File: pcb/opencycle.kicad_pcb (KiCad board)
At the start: 4 copper layers, 46 x 80 mm, 65 parts, among them J1 USB-C, J2 Battery, J3 LS027B7DH01, J4 SWD, SW1 Page/lap, SW2 Start/stop, SW3 Power, U1 MDBT50Q-1MV2, U10 SN74LV1T34DCK, U11 SN74LV1T34DCK, U12 BMP280, U13 LIS3DH, U14 MAX98357A, U2 MAX-M10S, U3 W25Q128JVSIQ, U4 MCP73831-2, U5 XC6220B331MR, U6 TPS61220DCK, U7 SN74LV1T34DCK, U8 SN74LV1T34DCK, U9 SN74LV1T34DCK

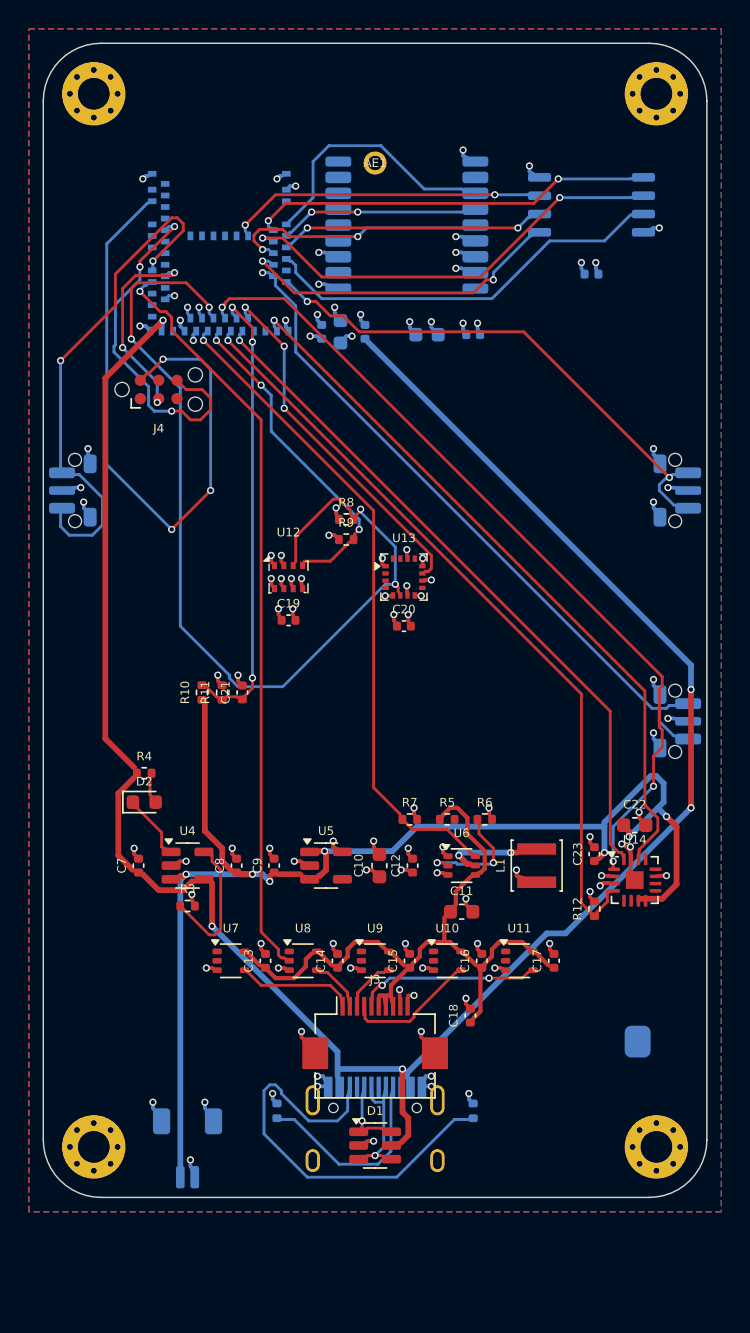
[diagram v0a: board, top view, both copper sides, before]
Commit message: pcb: text-generated local footprints (fixes pads stacked at the origin), work-in-progress routed board + DRC report
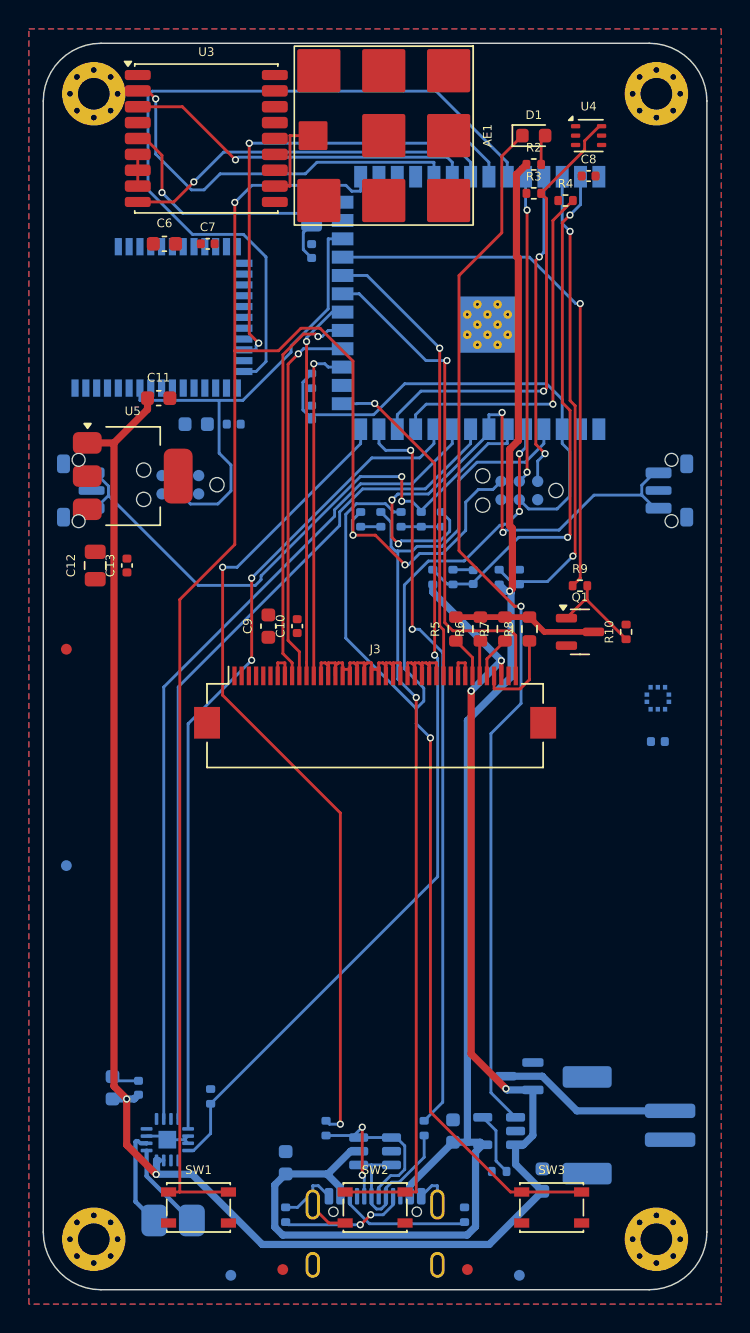
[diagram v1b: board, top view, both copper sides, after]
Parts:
- removed C21, C23: 100nF, C_0402_1005Metric
- removed C22: 10uF, C_0603_1608Metric
- removed L1: 4.7uH, L_Sunlord_SWPA3012S
- removed U10, U11, U9: SN74LV1T34DCK, SOT-353_SC-70-5
- removed U12: BMP280, Bosch_LGA-8_2x2.5mm_P0.65mm_ClockwisePinNumbering
- removed U13: LIS3DH, LGA-16_3x3mm_P0.5mm
- removed U14: MAX98357A, TQFN-16-1EP_3x3mm_P0.5mm_EP1.23x1.23mm
- added FID1: Fiducial, Fiducial_0.75mm_Mask1.5mm, F.Cu at (19.6, 88.0)
- added FID2: Fiducial, Fiducial_0.75mm_Mask1.5mm, F.Cu at (32.4, 88.0)
- added FID3: Fiducial, Fiducial_0.75mm_Mask1.5mm, F.Cu at (4.60, 45.0)
- added FID4: Fiducial, Fiducial_0.75mm_Mask1.5mm, B.Cu at (16.0, 88.4)
- added FID5: Fiducial, Fiducial_0.75mm_Mask1.5mm, B.Cu at (36.0, 88.4)
- added FID6: Fiducial, Fiducial_0.75mm_Mask1.5mm, B.Cu at (4.60, 60.0)
- added J5: Console, Tag-Connect_TC2030-IDC-NL_2x03_P1.27mm_Vertical, B.Cu at (36.0, 34.0)
- added Q1: DMG2302U, SOT-23, F.Cu at (40.2, 43.8)
- added Q2: DMG2305UX, SOT-23, B.Cu at (36.0, 74.6)
- added R13: 0R, R_0402_1005Metric, B.Cu at (22.6, 78.2)
- added R14: 0R, R_0402_1005Metric, B.Cu at (29.4, 78.2)
- added R15: 2k, R_0402_1005Metric, B.Cu at (34.6, 81.2)
- added R16: 1M, R_0402_1005Metric, B.Cu at (30.0, 40.0)
- added R17: 1M, R_0402_1005Metric, B.Cu at (31.4, 40.0)
- added R18: 100k, R_0402_1005Metric, B.Cu at (34.6, 40.0)
- added R19: 100k, R_0402_1005Metric, B.Cu at (36.0, 40.0)
- added R20: 100k, R_0402_1005Metric, B.Cu at (14.6, 76.0)
- added R21: 10k, R_0402_1005Metric, B.Cu at (25.0, 36.0)
- added R22: 10k, R_0402_1005Metric, B.Cu at (26.4, 36.0)
- added R23: 10k, R_0402_1005Metric, B.Cu at (27.8, 36.0)
- added R24: 10k, R_0402_1005Metric, B.Cu at (29.2, 36.0)
- added R25: 10k, R_0402_1005Metric, B.Cu at (30.6, 36.0)
- added SW4: SKRTLAE010, SW_Push_1P1T-MP_NO_Horizontal_Alps_SKRTLAE010, B.Cu at (5.45, 34.0)
- added SW5: SKRTLAE010, SW_Push_1P1T-MP_NO_Horizontal_Alps_SKRTLAE010, B.Cu at (46.5, 34.0)
- AE1: value GNSS patch 15x15x4 -> DSGP.1575.12.4.A.02; footprint Patch_15x15_Feed -> Taoglas_DSGP.1575.12.4.A.02_12x12mm
- C1: value 10uF -> 22uF; footprint C_0603_1608Metric -> C_0805_2012Metric
- C10: value 10uF -> 100nF; footprint C_0603_1608Metric -> C_0402_1005Metric
- C12: value 4.7uF -> 22uF; footprint C_0402_1005Metric -> C_0805_2012Metric
- C14, C15, C16: value 100nF -> 4.7uF; footprint C_0402_1005Metric -> C_0603_1608Metric; moved to B.Cu
- C17, C19, C20: moved to B.Cu
- C18: value 1uF -> 10uF; footprint C_0402_1005Metric -> C_0603_1608Metric; moved to B.Cu
- C3: value 4.7uF -> 1uF
- C6: value 100nF -> 10uF; footprint C_0402_1005Metric -> C_0603_1608Metric; moved to F.Cu
- C7, C8: value 4.7uF -> 100nF
- C9: value 1uF -> 10uF; footprint C_0402_1005Metric -> C_0603_1608Metric
- D1: value USBLC6-2SC6 -> Green; footprint SOT-23-6 -> LED_0603_1608Metric
- D2: value Green -> USBLC6-2SC6; footprint LED_0603_1608Metric -> SOT-23-6; moved to B.Cu
- J1: value USB-C -> USB4105-GF-A; footprint USB_C_Receptacle_HRO_TYPE-C-31-M-12 -> USB_C_Receptacle_GCT_USB4105-xx-A_16P_TopMnt_Horizontal
- J2: value Battery -> S2B-PH-SM4-TB; footprint JST_SH_SM02B-SRSS-TB_1x02-1MP_P1.00mm_Horizontal -> JST_PH_S2B-PH-SM4-TB_1x02-1MP_P2.00mm_Horizontal
- J3: value LS027B7DH01 -> FH12-40S-0.5SH(55); footprint Hirose_FH12-10S-0.5SH_1x10-1MP_P0.50mm_Horizontal -> Hirose_FH12-40S-0.5SH_1x40-1MP_P0.50mm_Horizontal
- J4: value SWD -> SWD (BL652); moved to B.Cu
- LS1: value 8R 1W 11x15 -> CMS-151125-078L100
- R1: value 5.1k -> 10k
- R10: value 1M -> 100k
- R11: value 1M -> 5.1k; moved to B.Cu
- R12: value 100k -> 5.1k; moved to B.Cu
- R2: value 5.1k -> 1k; moved to F.Cu
- R3: value 2k -> 4.7k
- R4: value 1k -> 4.7k
- R5, R7: value 1M -> 33R; footprint R_0402_1005Metric -> R_0603_1608Metric
- R6: value 110k -> 33R; footprint R_0402_1005Metric -> R_0603_1608Metric
- R8: value 4.7k -> 33R; footprint R_0402_1005Metric -> R_0603_1608Metric
- R9: value 4.7k -> 100R
- SW1: value Page/lap -> PTS810; footprint SW_Push_1P1T-MP_NO_Horizontal_Alps_SKRTLAE010 -> SW_SPST_PTS810; moved to F.Cu
- SW2: value Start/stop -> PTS810; footprint SW_Push_1P1T-MP_NO_Horizontal_Alps_SKRTLAE010 -> SW_SPST_PTS810; moved to F.Cu
- SW3: value Power -> PTS810; footprint SW_Push_1P1T-MP_NO_Horizontal_Alps_SKRTLAE010 -> SW_SPST_PTS810; moved to F.Cu
- U1: value MDBT50Q-1MV2 -> ESP32-S3-WROOM-1-N16R8; footprint Raytac_MDBT50Q -> ESP32-S3-WROOM-1
- U2: value MAX-M10S -> BL652-SA-01; footprint ublox_MAX -> Laird_BL652
- U3: value W25Q128JVSIQ -> MAX-M10S; footprint SOIC-8_5.23x5.23mm_P1.27mm -> ublox_MAX; moved to F.Cu
- U4: value MCP73831-2 -> LTR-303ALS-01; footprint SOT-23-5 -> Lite-On_LTR-303ALS-01
- U5: value XC6220B331MR -> AP7361C-33E; footprint SOT-23-5 -> SOT-223-3_TabPin2
- U6: value TPS61220DCK -> MCP73831-2; footprint SOT-363_SC-70-6 -> SOT-23-5; moved to B.Cu
- U7: value SN74LV1T34DCK -> MAX98357A; footprint SOT-353_SC-70-5 -> TQFN-16-1EP_3x3mm_P0.5mm_EP1.23x1.23mm; moved to B.Cu
- U8: value SN74LV1T34DCK -> BMP581; footprint SOT-353_SC-70-5 -> Bosch_LGA-10_2x2mm_P0.5mm_BMP581; moved to B.Cu
- moved D1 70.9 mm to (37.0, 9.40)
- moved R2 65.7 mm to (37.0, 11.4), turned to 0 degrees
- moved SW1 59.7 mm to (13.8, 83.7), turned to 0 degrees
- moved SW3 59.7 mm to (38.2, 83.7), turned to 0 degrees
- moved U4 57.7 mm to (40.8, 9.40)
- moved R3 54.9 mm to (37.0, 13.4)
- moved C8 53.7 mm to (40.8, 12.2), turned to 0 degrees
- moved R1 50.7 mm to (21.6, 26.4)
- moved R4 49.3 mm to (39.2, 13.9)
- moved C7 43.4 mm to (14.4, 16.9), turned to 0 degrees
- moved C11 41.3 mm to (11.0, 27.6)
- moved SW2 39.6 mm to (26.0, 83.7), turned to 0 degrees
- moved R11 36.5 mm to (19.8, 84.2)
- moved LS1 34.5 mm to (12.0, 84.6)
- moved C19 34.0 mm to (9.60, 75.4), turned to 90 degrees
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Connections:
- C11 pad 1: +5V_DISP -> VBAT
- C13 pad 1: +5V_DISP -> +3V3
- C14 pad 1: +5V_DISP -> VBUS
- C15 pad 1: +5V_DISP -> VBUS
- C16 pad 1: +5V_DISP -> VBAT
- C17 pad 1: +5V_DISP -> VBAT_SENSE
- C18 pad 1: +5V_DISP -> VBAT
- C19 pad 1: +3V3 -> VBAT
- C3 pad 1: VBUS -> ESP_EN
- C7 pad 1: VBUS -> +3V3
- C8 pad 1: VBAT -> +3V3
- C9 pad 1: VBAT -> +3V3
- D1 pad 1: USB_DP_C -> CHG_STAT
- D1 pad 2: GND -> LED_A
- D2 pad 1: CHG_STAT -> USB_DP_C
- D2 pad 2: LED_A -> GND
- J2 pad 1: VBAT -> GND
- J2 pad 2: GND -> BATT+
- J3 pad 1: DISP_SCLK -> GND
- J3 pad 10: GND -> LCD_CS
- J3 pad 2: DISP_SI -> (no net)
- J3 pad 3: DISP_SCS -> (no net)
- J3 pad 4: DISP_EXTCOM -> (no net)
- J3 pad 5: DISP_ON -> (no net)
- J3 pad 6: +5V_DISP -> (no net)
- J3 pad 7: +5V_DISP -> +3V3
- J3 pad 8: +5V_DISP -> +3V3
- J3 pad 9: GND -> LCD_MOSI
- J4 pad 2: SWDIO -> BLE_SWDIO
- J4 pad 3: ~RESET -> BLE_RST
- J4 pad 4: SWDCLK -> BLE_SWDCLK
- J4 pad 6: SWO -> (no net)
- R1 pad 1: CC1 -> +3V3
- R1 pad 2: GND -> ESP_EN
- R10 pad 1: VBAT -> BL_G
- R10 pad 2: VBAT_SENSE -> GND
- R11 pad 1: VBAT_SENSE -> CC1
- R12 pad 1: AMP_EN -> CC2
- R2 pad 1: CC2 -> VBUS
- R2 pad 2: GND -> LED_A
- R3 pad 1: CHG_PROG -> +3V3
- R3 pad 2: GND -> I2C_SDA
- R4 pad 1: VBUS -> +3V3
- R4 pad 2: LED_A -> I2C_SCL
- R5 pad 1: +5V_DISP -> LED_K1
- R5 pad 2: BOOST_FB -> BL_SW
- R6 pad 1: BOOST_FB -> LED_K2
- R6 pad 2: GND -> BL_SW
- R7 pad 1: DISP_PWR_EN -> LED_K3
- R7 pad 2: GND -> BL_SW
- R8 pad 1: +3V3 -> LED_K4
- R8 pad 2: I2C_SDA -> BL_SW
- R9 pad 1: +3V3 -> LCD_BL
- R9 pad 2: I2C_SCL -> BL_G
- SW1 pad 1: BTN_PAGE -> KEY_L
- SW2 pad 1: BTN_START -> KEY_C
- SW3 pad 1: BTN_POWER -> KEY_R
- U1 pad 10: FLASH_IO2 -> I2S_DIN
- U1 pad 11: FLASH_IO0 -> I2C_SCL
- U1 pad 12: GNSS_RST -> I2C_SDA
- U1 pad 13: BTN_START -> USB_DN
- U1 pad 14: BTN_PAGE -> USB_DP
- U1 pad 15: GND -> AMP_EN
- U1 pad 16: I2S_LRCLK -> (no net)
- U1 pad 17: (no net) -> LCD_DC
- U1 pad 18: (no net) -> LCD_CS
- U1 pad 19: IMU_INT1 -> LCD_MOSI
- U1 pad 2: GND -> +3V3
- U1 pad 20: I2S_BCLK -> LCD_SCK
- U1 pad 21: VBAT_SENSE -> LCD_TE
- U1 pad 22: AMP_EN -> LCD_RST
- U1 pad 23: I2S_DIN -> LCD_BL
- U1 pad 24: I2C_SCL -> BLE_RST
- U1 pad 25: I2C_SDA -> GPS_EXTINT
- U1 pad 26: DISP_PWR_EN -> (no net)
- U1 pad 27: DISP_ON_3V -> KEY_L
- U1 pad 28: +3V3 -> (no net)
- U1 pad 29: DISP_EXTCOM_3V -> (no net)
- U1 pad 3: GNSS_TXD -> ESP_EN
- U1 pad 30: +3V3 -> (no net)
- U1 pad 31: (no net) -> GPS_TX
- U1 pad 32: VBUS -> GPS_RX
- U1 pad 33: GND -> GPS_RST
- U1 pad 34: USB_DN -> BLE_TX
- U1 pad 35: USB_DP -> BLE_RX
- U1 pad 36: DISP_SCS_3V -> CON_RX
- U1 pad 37: DISP_SCLK_3V -> CON_TX
- U1 pad 38: (no net) -> VBUS_SENSE
- U1 pad 39: DISP_SI_3V -> VBAT_SENSE
- U1 pad 4: GNSS_RXD -> KEY_C
- U1 pad 40: ~RESET -> GND
- U1 pad 41: BTN_POWER -> GND
- U1 pad 5: FLASH_CS -> KEY_R
- U1 pad 6: GNSS_PPS -> BTN_PWR
- U1 pad 7: FLASH_IO1 -> BTN_MENU
- U1 pad 8: FLASH_CLK -> I2S_BCLK
- U1 pad 9: GNSS_EXTINT -> I2S_LRCLK
- U2 pad 10: GND -> (no net)
- U2 pad 11: RF_IN -> (no net)
- U2 pad 12: GND -> (no net)
- U2 pad 16: (no net) -> GND
- U2 pad 17: (no net) -> BLE_RX
- U2 pad 2: GNSS_TXD -> (no net)
- U2 pad 3: GNSS_RXD -> (no net)
- U2 pad 4: GNSS_PPS -> (no net)
- U2 pad 5: GNSS_EXTINT -> BLE_SWDIO
- U2 pad 6: +3V3 -> BLE_SWDCLK
- U2 pad 7: +3V3 -> BLE_RST
- U2 pad 8: +3V3 -> (no net)
- U2 pad 9: GNSS_RST -> (no net)
- U3 pad 1: FLASH_CS -> GND
- U3 pad 2: FLASH_IO1 -> GPS_TX
- U3 pad 3: FLASH_IO2 -> GPS_RX
- U3 pad 4: GND -> (no net)
- U3 pad 5: FLASH_IO0 -> GPS_EXTINT
- U3 pad 6: FLASH_CLK -> +3V3
- U3 pad 7: FLASH_IO3 -> +3V3
- U4 pad 1: CHG_STAT -> +3V3
- U4 pad 2: GND -> (no net)
- U4 pad 3: VBAT -> GND
- U4 pad 4: VBUS -> I2C_SCL
- U4 pad 5: CHG_PROG -> (no net)
- U5 pad 3: VBAT -> +3V3
- U6 pad 1: +3V3 -> CHG_STAT
- U6 pad 2: BOOST_FB -> GND
- U6 pad 3: GND -> VBAT
- U6 pad 4: +5V_DISP -> VBUS
- U6 pad 5: BOOST_SW -> CHG_PROG
- U7 pad 1: (no net) -> I2S_DIN
- U7 pad 2: DISP_SCLK_3V -> GND
- U7 pad 4: DISP_SCLK -> AMP_EN
- U7 pad 5: +5V_DISP -> (no net)
- U8 pad 1: (no net) -> +3V3
- U8 pad 2: DISP_SI_3V -> I2C_SCL
- U8 pad 4: DISP_SI -> I2C_SDA
- U8 pad 5: +5V_DISP -> GND
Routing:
- net KEY_L: track 0.00 -> 123.1 mm, vias 0 -> 3
- net KEY_R: track 0.00 -> 86.3 mm, vias 0 -> 3
- net KEY_C: track 0.00 -> 69.4 mm, vias 0 -> 1
- net CHG_STAT: track 4.65 -> 73.5 mm, vias 0 -> 1
- net USB_DP: track 0.00 -> 57.2 mm, vias 0 -> 2
- net BLE_RX: track 0.00 -> 53.8 mm
- net +5V_DISP: track 52.7 -> 0.00 mm
- net DISP_SI_3V: track 52.2 -> 0.00 mm, vias 1 -> 0
- net USB_DN: track 0.00 -> 51.6 mm, vias 0 -> 2
- net VBAT: track 93.0 -> 141.9 mm, vias 7 -> 5
- net BTN_START: track 47.6 -> 0.00 mm, vias 1 -> 0
- net DISP_PWR_EN: track 45.8 -> 0.00 mm, vias 1 -> 0
- net SWDIO: track 44.0 -> 0.00 mm, vias 3 -> 0
- net BTN_MENU: track 0.00 -> 42.4 mm, vias 0 -> 4
- net BTN_PWR: track 0.00 -> 42.2 mm, vias 0 -> 2
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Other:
- board size 46 x 80 mm -> 46 x 86.4 mm
- board text added: "OpenCycle v0.2"
- board text added: "github.com/Vishvak365/OpenCycle"
- board text added: "rev A 2026-09"
- board text removed: "OpenCycle v0.1"

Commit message: pcb: plane fan-out, dangling clean-up, GND stitching + island vias, custom DRC rules; board down to 2 unrouted (BMP581 I2C)
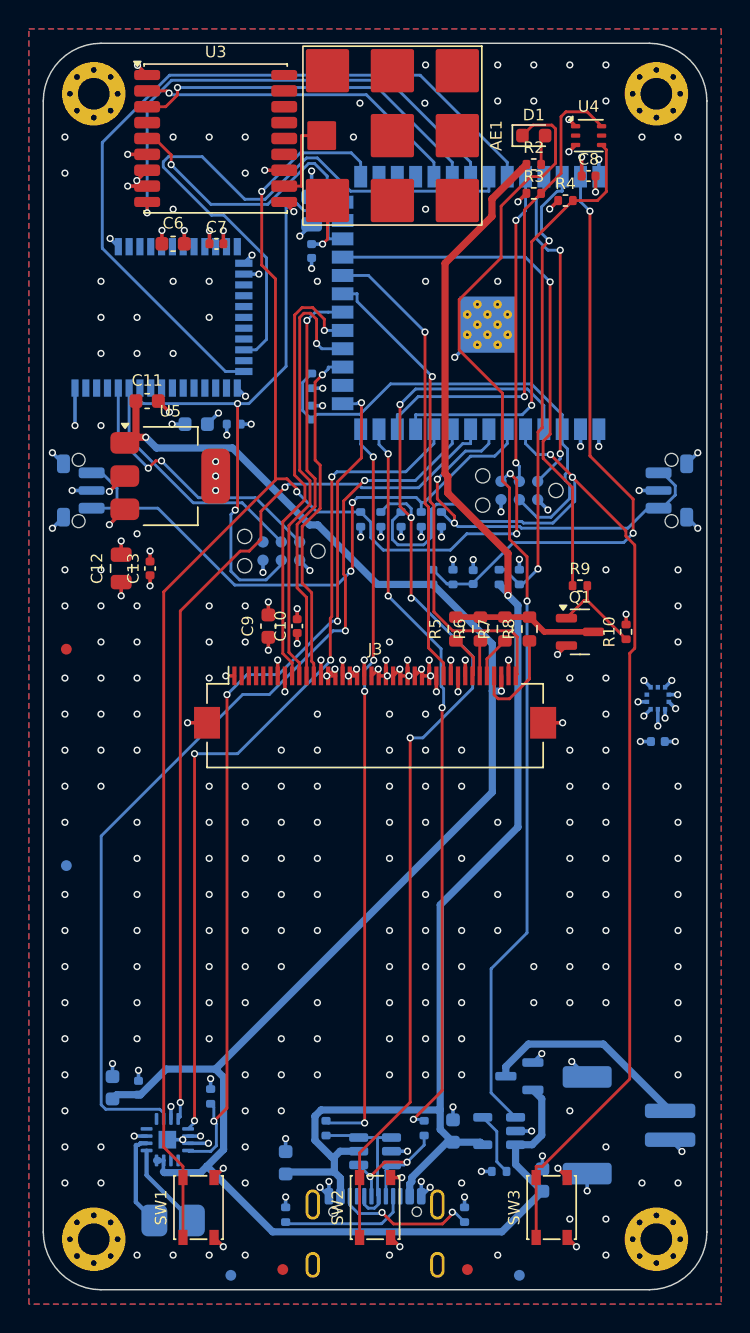
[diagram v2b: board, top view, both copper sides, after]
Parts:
- moved J4 8.38 mm to (19.5, 38.2)
- moved U5 2.60 mm to (11.8, 33.0)
- moved C12 1.81 mm to (8.40, 39.4)
- moved C13 1.61 mm to (10.4, 39.4)
- moved C11 0.82 mm to (10.2, 27.8)
- moved U3 0.65 mm to (14.9, 9.60)
- moved C6 0.60 mm to (12.0, 16.9)
- moved C7 0.60 mm to (15.0, 16.9)
- moved AE1 0.60 mm to (27.2, 9.40)
- turned SW1 to 90 degrees
- turned SW2 to 90 degrees
- turned SW3 to 90 degrees
- turned U8 to 0 degrees
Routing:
- net GND: track 41.7 -> 96.4 mm, vias 0 -> 295
- net +3V3: track 13.8 -> 33.4 mm, vias 0 -> 36
- net BLE_SWDIO: track 0.00 -> 19.4 mm, vias 0 -> 2
- net BLE_SWDCLK: track 0.00 -> 17.0 mm
- net BTN_MENU: track 42.4 -> 28.9 mm, vias 4 -> 2
- net VBAT: track 141.9 -> 128.9 mm, vias 5 -> 2
- net KEY_L: track 123.1 -> 111.1 mm, vias 3 -> 4
- net BLE_RST: track 33.4 -> 45.3 mm, vias 0 -> 2
- net BLE_TX: track 33.7 -> 44.7 mm, vias 2 -> 0
- net KEY_C: track 69.4 -> 79.4 mm, vias 1 -> 4
- net GPS_RST: track 25.8 -> 34.7 mm
- net I2S_LRCLK: track 58.2 -> 65.7 mm, vias 0 -> 2
- net VBUS: track 109.8 -> 103.7 mm
- net USB_DP: track 57.2 -> 51.5 mm, vias 2 -> 4
- net I2C_SCL: track 25.5 -> 30.6 mm
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
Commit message: pcb: v0.2 board fully routed - DRC 0 errors, 0 unconnected (5 intentional warnings); refs on fab layer, lib tables; cad: rotated key switches, board_fit OK on the routed board
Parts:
- AE1: footprint Taoglas_DSGP.1575.12.4.A.02_12x12mm -> OpenCycle:Taoglas_DSGP.1575.12.4.A.02_12x12mm
- C1, C12: footprint C_0805_2012Metric -> Capacitor_SMD:C_0805_2012Metric
- C10, C13, C17, C19, C2, C20, C3, C5, C7, C8: footprint C_0402_1005Metric -> Capacitor_SMD:C_0402_1005Metric
- C11, C14, C15, C16, C18, C4, C6, C9: footprint C_0603_1608Metric -> Capacitor_SMD:C_0603_1608Metric
- D1: footprint LED_0603_1608Metric -> LED_SMD:LED_0603_1608Metric
- D2: footprint SOT-23-6 -> Package_TO_SOT_SMD:SOT-23-6
- FID1, FID2, FID3, FID4, FID5, FID6: footprint Fiducial_0.75mm_Mask1.5mm -> Fiducial:Fiducial_0.75mm_Mask1.5mm
- H1, H2, H3, H4: footprint MountingHole_2.2mm_M2_Pad_Via -> MountingHole:MountingHole_2.2mm_M2_Pad_Via
- J1: footprint USB_C_Receptacle_GCT_USB4105-xx-A_16P_TopMnt_Horizontal -> Connector_USB:USB_C_Receptacle_GCT_USB4105-xx-A_16P_TopMnt_Horizontal
- J2: footprint JST_PH_S2B-PH-SM4-TB_1x02-1MP_P2.00mm_Horizontal -> Connector_JST:JST_PH_S2B-PH-SM4-TB_1x02-1MP_P2.00mm_Horizontal
- J3: footprint Hirose_FH12-40S-0.5SH_1x40-1MP_P0.50mm_Horizontal -> Connector_FFC-FPC:Hirose_FH12-40S-0.5SH_1x40-1MP_P0.50mm_Horizontal
- J4, J5: footprint Tag-Connect_TC2030-IDC-NL_2x03_P1.27mm_Vertical -> Connector:Tag-Connect_TC2030-IDC-NL_2x03_P1.27mm_Vertical
- LS1: footprint SpeakerPads_2.6mm -> OpenCycle:SpeakerPads_2.6mm
- Q1, Q2: footprint SOT-23 -> Package_TO_SOT_SMD:SOT-23
- R1, R10, R11, R12, R13, R14, R15, R16, R17, R18, R19, R2, R20, R21, R22, R23, R24, R25, R3, R4, R9: footprint R_0402_1005Metric -> Resistor_SMD:R_0402_1005Metric
- R5, R6, R7, R8: footprint R_0603_1608Metric -> Resistor_SMD:R_0603_1608Metric
- SW1, SW2, SW3: footprint SW_SPST_PTS810 -> Button_Switch_SMD:SW_SPST_PTS810
- SW4, SW5: footprint SW_Push_1P1T-MP_NO_Horizontal_Alps_SKRTLAE010 -> Button_Switch_SMD:SW_Push_1P1T-MP_NO_Horizontal_Alps_SKRTLAE010
- U1: footprint ESP32-S3-WROOM-1 -> RF_Module:ESP32-S3-WROOM-1
- U2: footprint Laird_BL652 -> RF_Module:Laird_BL652
- U3: footprint ublox_MAX -> RF_GPS:ublox_MAX
- U4: footprint Lite-On_LTR-303ALS-01 -> OptoDevice:Lite-On_LTR-303ALS-01
- U5: footprint SOT-223-3_TabPin2 -> Package_TO_SOT_SMD:SOT-223-3_TabPin2
- U6: footprint SOT-23-5 -> Package_TO_SOT_SMD:SOT-23-5
- U7: footprint TQFN-16-1EP_3x3mm_P0.5mm_EP1.23x1.23mm -> Package_DFN_QFN:TQFN-16-1EP_3x3mm_P0.5mm_EP1.23x1.23mm
- U8: footprint Bosch_LGA-10_2x2mm_P0.5mm_BMP581 -> OpenCycle:Bosch_LGA-10_2x2mm_P0.5mm_BMP581
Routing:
- net I2C_SDA: track 34.2 -> 68.0 mm, vias 1 -> 2
- net I2C_SCL: track 30.6 -> 59.0 mm, vias 1 -> 2
- net KEY_L: track 111.1 -> 94.2 mm
- net VBAT: track 128.9 -> 141.2 mm, vias 2 -> 3
- net USB_DP: track 51.5 -> 63.1 mm, vias 4 -> 2
- net KEY_R: track 83.0 -> 91.6 mm, vias 2 -> 4
- net BTN_PWR: track 43.3 -> 51.3 mm
- net GPS_RST: track 34.7 -> 26.9 mm
- net I2S_LRCLK: track 65.7 -> 58.4 mm, vias 2 -> 0
- net VBAT_SENSE: track 42.0 -> 34.8 mm
- net LCD_CS: track 31.1 -> 25.3 mm
- net ESP_EN: track 33.7 -> 38.9 mm
- net CHG_STAT: track 78.2 -> 73.3 mm, vias 1 -> 3
- net KEY_C: track 79.4 -> 74.8 mm, vias 4 -> 1
- net LCD_MOSI: track 30.9 -> 26.6 mm
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
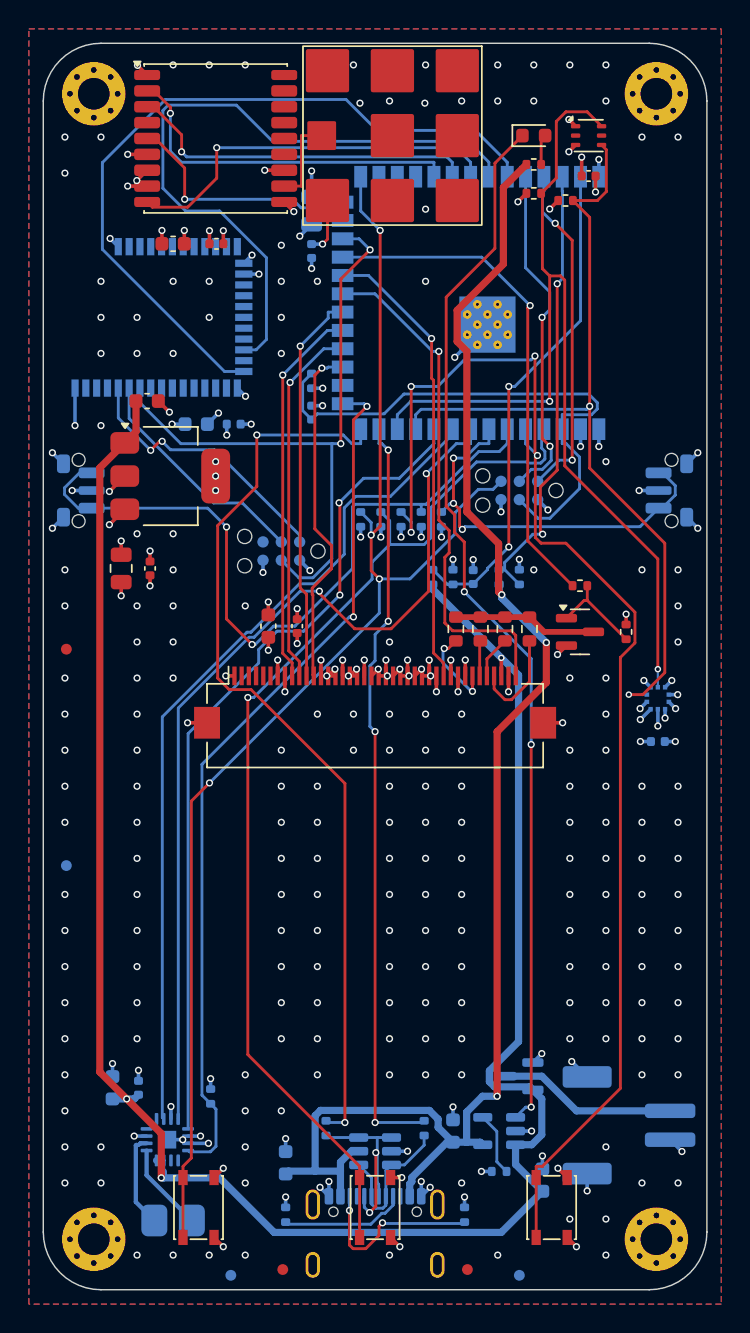
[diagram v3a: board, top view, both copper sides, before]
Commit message: Product page, v0.2 README, full pipeline rebuild
- viewer/product.html: photoreal scroll-driven tour of the real CAD case and
  routed board, live Lucent UI with working soft keys, specs, build steps
- README rewritten for v0.2 (status, build steps, renders)
- tools/build_all.sh run end to end: fit OK, placement OK, DRC 0 errors /
  0 unconnected, netlist match, board fit OK; regenerated fab, print, viewer
  and time-lapse outputs (GPS patch at x 27.2)
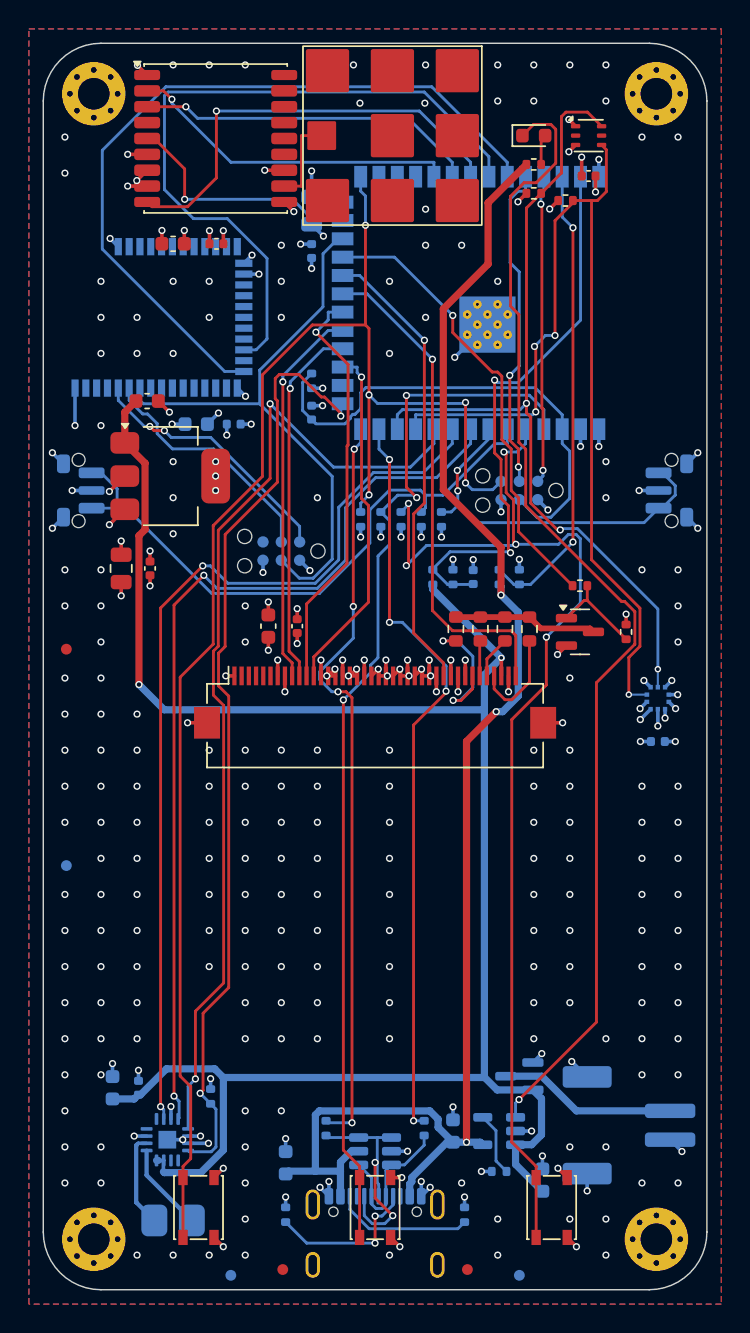
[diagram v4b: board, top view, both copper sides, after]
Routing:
- net KEY_L: track 94.2 -> 110.4 mm, vias 4 -> 5
- net KEY_R: track 91.6 -> 78.8 mm, vias 4 -> 5
- net USB_DP: track 63.1 -> 52.7 mm, vias 2 -> 4
- net I2S_DIN: track 58.1 -> 68.1 mm
- net I2C_SCL: track 59.0 -> 68.8 mm, vias 2 -> 4
- net I2C_SDA: track 68.0 -> 58.9 mm, vias 2 -> 3
- net BTN_PWR: track 51.3 -> 43.1 mm, vias 2 -> 0
- net CHG_STAT: track 73.3 -> 80.2 mm, vias 3 -> 1
- net VBAT: track 141.2 -> 134.5 mm, vias 3 -> 2
- net I2S_LRCLK: track 58.4 -> 64.6 mm, vias 0 -> 2
- net AMP_EN: track 60.5 -> 65.6 mm
- net VBAT_SENSE: track 34.8 -> 39.4 mm
- net ESP_EN: track 38.9 -> 34.3 mm
- net BLE_RST: track 45.2 -> 40.7 mm, vias 2 -> 0
- net LED_K1: track 5.99 -> 9.87 mm
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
